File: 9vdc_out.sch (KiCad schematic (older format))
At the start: 3 parts, among them U2 LM7809_TO220

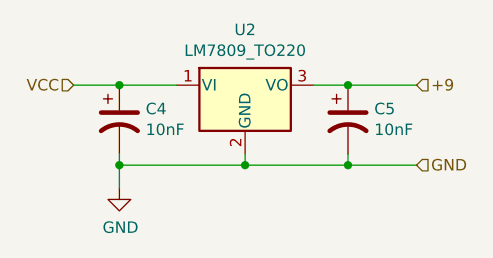
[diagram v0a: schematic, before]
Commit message: Fixed ERC errors, combined all outputs into a bus, fixed annotations
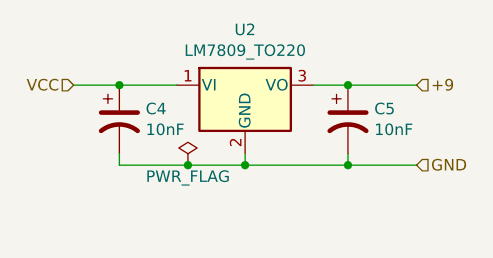
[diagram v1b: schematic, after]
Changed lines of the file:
@@
 	7400 3250 7400 3200
-Wire Wire Line
-	6950 3250 6400 3250
 Wire Wire Line
 	6400 3250 6400 3200
@@
 	1    0    0    -1
 $EndComp
+Wire Wire Line
+	6400 3250 6700 3250
 $Comp
-L power:GND #PWR0104
-U 1 1 5E70EC51
-P 6400 3350
-F 0 "#PWR0104" H 6400 3100 50  0001 C CNN
-F 1 "GND" H 6405 3177 50  0000 C CNN
-F 2 "" H 6400 3350 50  0001 C CNN
-F 3 "" H 6400 3350 50  0001 C CNN
-	1    6400 3350
+L power:PWR_FLAG #FLG0102
+U 1 1 5E7290D2
+P 6700 3250
+F 0 "#FLG0102" H 6700 3325 50  0001 C CNN
+F 1 "PWR_FLAG" H 6700 3200 50  0000 C CNN
+F 2 "" H 6700 3250 50  0001 C CNN
+F 3 "~" H 6700 3250 50  0001 C CNN
+	1    6700 3250
 	1    0    0    -1
 $EndComp
+Connection ~ 6700 3250
 Wire Wire Line
-	6400 3350 6400 3250
-Connection ~ 6400 3250
+	6700 3250 6950 3250
 $EndSCHEMATC
